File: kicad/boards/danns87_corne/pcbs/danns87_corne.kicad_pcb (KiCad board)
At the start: 2 copper layers, 132 x 85.7 mm, 46 parts

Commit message: danns87_corne: Almost functional
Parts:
- moved MCU1 15.7 mm to (128.4, -11.5)
- moved ? 15.5 mm to (135.7, 7.09), turned to 150 degrees
- turned ? to 0 degrees
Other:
- board size 132 x 85.7 mm -> 132.4 x 88 mm

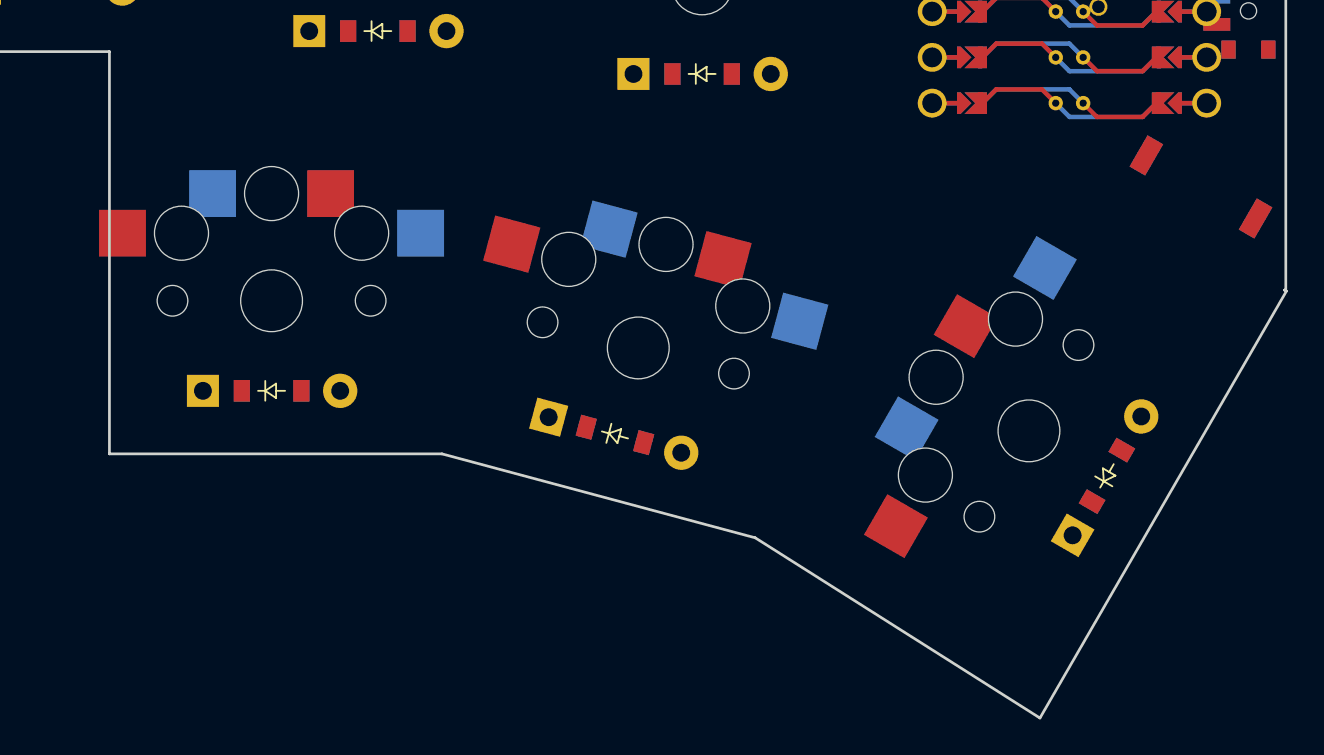
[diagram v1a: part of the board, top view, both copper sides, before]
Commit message: danns87_corne: Perfectly matching Chocorne key switches positions
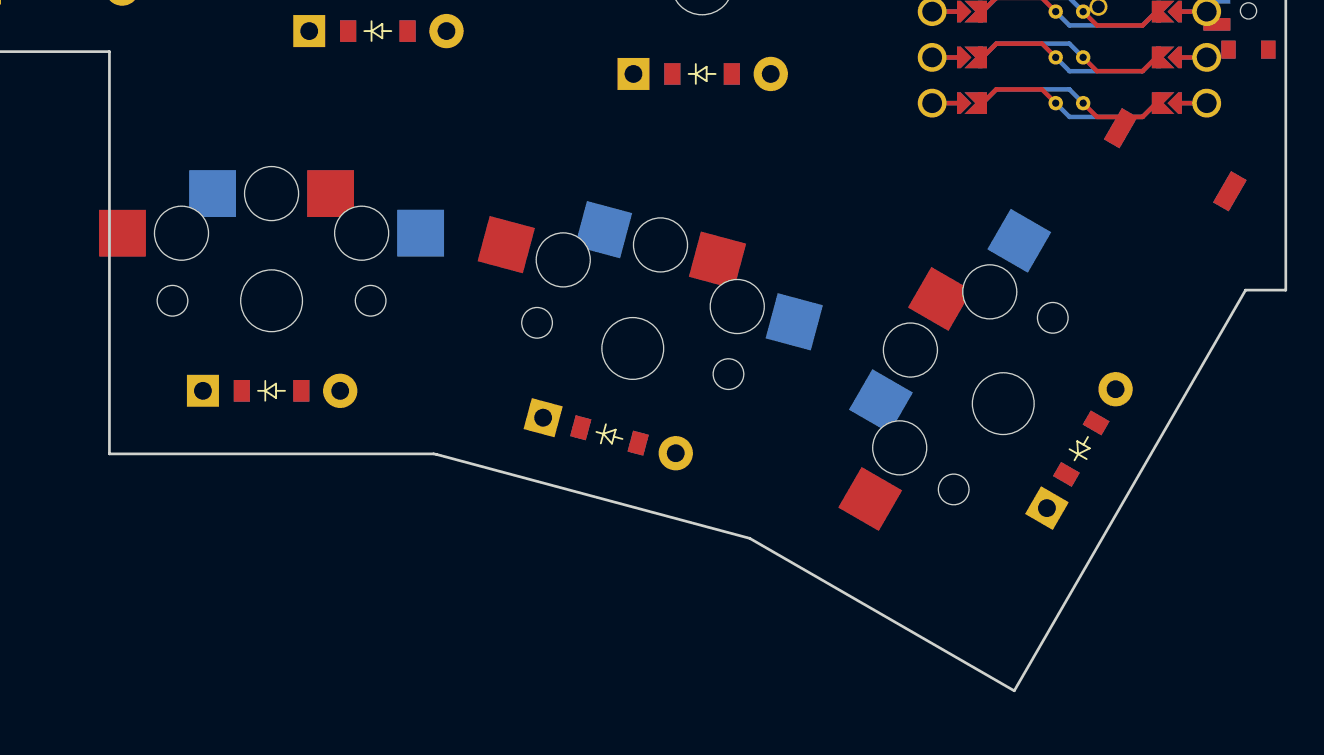
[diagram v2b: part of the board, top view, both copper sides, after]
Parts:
- moved D21 2.08 mm to (129.0, 21.6)
- moved S21 2.08 mm to (124.7, 19.1)
- moved ? 2.08 mm to (134.3, 5.58)
- moved S20 0.31 mm to (104.2, 16.1)
- moved D20 0.31 mm to (102.9, 20.9)
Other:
- board size 132.4 x 88 mm -> 132.4 x 86.5 mm
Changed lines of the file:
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@@
     )
       (module PG1350 (layer F.Cu)
-      (at 104.4562943 16.0290019 -15)
+      (at 104.15029429999998 16.0580019 -15)
       (fp_text reference "S20" (at 0 0) (layer F.SilkS) hide (effects (font (size 1.27 1.27) (thickness 0.15))))
       (fp_text value "" (at 0 0) (layer F.SilkS) hide (effects (font (size 1.27 1.27) (thickness 0.15))))
@@
         )
     (module ComboDiode (layer F.Cu)
-        (at 103.1621991 20.858631000000003 -15)
+        (at 102.85619909999998 20.887631 -15)
         (fp_text reference "D20" (at 0 0) (layer F.SilkS) hide (effects (font (size 1.27 1.27) (thickness 0.15))))
         (fp_text value "" (at 0 0) (layer F.SilkS) hide (effects (font (size 1.27 1.27) (thickness 0.15))))
@@
     )
       (module PG1350 (layer F.Cu)
-      (at 126.14228589999999 20.6315805 60)
+      (at 124.71581489999998 19.120090299999998 60)
       (fp_text reference "S21" (at 0 0) (layer F.SilkS) hide (effects (font (size 1.27 1.27) (thickness 0.15))))
       (fp_text value "" (at 0 0) (layer F.SilkS) hide (effects (font (size 1.27 1.27) (thickness 0.15))))
@@
         )
     (module ComboDiode (layer F.Cu)
-        (at 130.4724129 23.1315805 60)
+        (at 129.04594189999997 21.620090299999998 60)
         (fp_text reference "D21" (at 0 0) (layer F.SilkS) hide (effects (font (size 1.27 1.27) (thickness 0.15))))
         (fp_text value "" (at 0 0) (layer F.SilkS) hide (effects (font (size 1.27 1.27) (thickness 0.15))))
@@
           )
 	(module Button_Switch_SMD:SW_SPST_UXCELL (layer F.Cu)
-        (at 135.69132399999998 7.092161299999999 150)
+        (at 134.264853 5.580671099999998 150)
 	  (descr "uxcell 3x6x4mm Momentary PCB SMT Surface Mounted Devices Rectangle Push Button SPST Tactile Tact Switch White 20PCS")
 	  (tags "Tactile Switch")
@@
 (gr_line (start 118 -29.68) (end 118 -46.68) (angle 90) (layer Edge.Cuts) (width 0.15))
 (gr_line (start 100 -46.68) (end 118 -46.68) (angle 90) (layer Edge.Cuts) (width 0.15))
-(gr_line (start 75.1 21.91) (end 93.56299999999999 21.91) (angle 90) (layer Edge.Cuts) (width 0.15))
+(gr_line (start 75.1 21.91) (end 93.1 21.91) (angle 90) (layer Edge.Cuts) (width 0.15))
 (gr_line (start 75.1 21.91) (end 75.1 -0.41999999999999993) (angle 90) (layer Edge.Cuts) (width 0.15))
-(gr_line (start 93.56299999999999 21.91) (end 110.9496649 26.568742800000003) (angle 90) (layer Edge.Cuts) (width 0.15))
-(gr_line (start 126.7535018 36.5729235) (end 140.4335018 12.8784684) (angle 90) (layer Edge.Cuts) (width 0.15))
-(gr_line (start 110.9496649 26.568742800000003) (end 126.7535018 36.5729235) (angle 90) (layer Edge.Cuts) (width 0.15))
-(gr_line (start 140.4335018 12.8784684) (end 140.32709037192762 12.819999999999993) (angle 90) (layer Edge.Cuts) (width 0.15))
-(gr_line (start 140.32709037192762 12.82) (end 140.4 12.82) (angle 90) (layer Edge.Cuts) (width 0.15))
+(gr_line (start 93.25699999999998 21.939) (end 110.64366489999999 26.5977428) (angle 90) (layer Edge.Cuts) (width 0.15))
+(gr_line (start 125.32703079999999 35.0614333) (end 138.16812827448888 12.819999999999965) (angle 90) (layer Edge.Cuts) (width 0.15))
+(gr_line (start 93.1 21.91) (end 93.25699999999998 21.939) (angle 90) (layer Edge.Cuts) (width 0.15))
+(gr_line (start 110.64366489999999 26.5977428) (end 125.32703079999999 35.0614333) (angle 90) (layer Edge.Cuts) (width 0.15))
+(gr_line (start 138.16812827448888 12.82) (end 140.4 12.82) (angle 90) (layer Edge.Cuts) (width 0.15))
 (gr_line (start 140.4 12.82) (end 140.4 -29.68) (angle 90) (layer Edge.Cuts) (width 0.15))
 (gr_line (start 140.4 -29.68) (end 118 -29.68) (angle 90) (layer Edge.Cuts) (width 0.15))
@@
 (gr_line (start 92.85 5.16) (end 75.35 5.16) (angle 90) (layer Eco1.User) (width 0.15))
 (gr_line (start 75.35 5.16) (end 75.35 21.66) (angle 90) (layer Eco1.User) (width 0.15))
-(gr_line (start 93.8691862 21.7332233) (end 110.7728882 26.2625566) (angle 90) (layer Eco1.User) (width 0.15))
-(gr_line (start 110.7728882 26.2625566) (end 115.04340239999999 10.324780500000001) (angle 90) (layer Eco1.User) (width 0.15))
-(gr_line (start 115.04340239999999 10.324780500000001) (end 98.1397004 5.795447200000002) (angle 90) (layer Eco1.User) (width 0.15))
-(gr_line (start 98.1397004 5.795447200000002) (end 93.8691862 21.7332233) (angle 90) (layer Eco1.User) (width 0.15))
-(gr_line (start 126.66199549999999 36.2314171) (end 139.9119955 13.281743899999999) (angle 90) (layer Eco1.User) (width 0.15))
-(gr_line (start 139.9119955 13.281743899999999) (end 125.62257629999999 5.031743899999999) (angle 90) (layer Eco1.User) (width 0.15))
-(gr_line (start 125.62257629999999 5.031743899999999) (end 112.37257629999999 27.981417099999998) (angle 90) (layer Eco1.User) (width 0.15))
-(gr_line (start 112.37257629999999 27.981417099999998) (end 126.66199549999999 36.2314171) (angle 90) (layer Eco1.User) (width 0.15))
+(gr_line (start 93.56318619999999 21.762223300000002) (end 110.46688819999999 26.2915566) (angle 90) (layer Eco1.User) (width 0.15))
+(gr_line (start 110.46688819999999 26.2915566) (end 114.73740239999998 10.353780500000001) (angle 90) (layer Eco1.User) (width 0.15))
+(gr_line (start 114.73740239999998 10.353780500000001) (end 97.83370039999998 5.824447200000002) (angle 90) (layer Eco1.User) (width 0.15))
+(gr_line (start 97.83370039999998 5.824447200000002) (end 93.56318619999999 21.762223300000002) (angle 90) (layer Eco1.User) (width 0.15))
+(gr_line (start 125.23552449999998 34.7199269) (end 138.4855245 11.770253699999998) (angle 90) (layer Eco1.User) (width 0.15))
+(gr_line (start 138.4855245 11.770253699999998) (end 124.19610529999999 3.520253699999998) (angle 90) (layer Eco1.User) (width 0.15))
+(gr_line (start 124.19610529999999 3.520253699999998) (end 110.94610529999999 26.469926899999997) (angle 90) (layer Eco1.User) (width 0.15))
+(gr_line (start 110.94610529999999 26.469926899999997) (end 125.23552449999998 34.7199269) (angle 90) (layer Eco1.User) (width 0.15))
 )
